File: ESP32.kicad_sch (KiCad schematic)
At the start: 5 parts, among them U1 ESP32-S3-WROOM-1

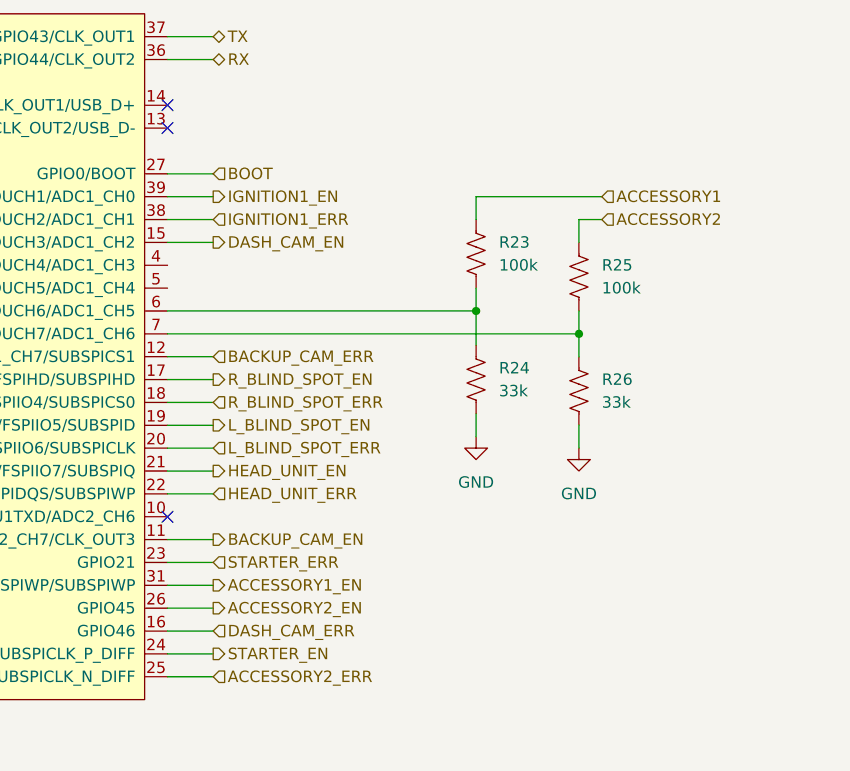
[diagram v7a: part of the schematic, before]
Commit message: add LED for debugging
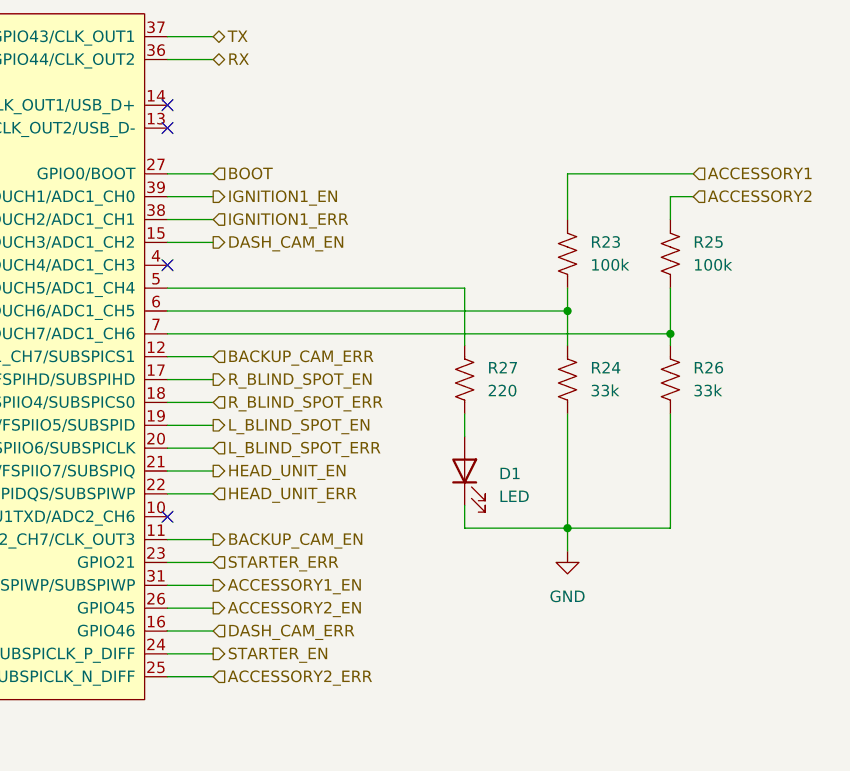
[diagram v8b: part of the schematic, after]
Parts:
- added D1: LED, LED_SMD:LED_0603_1608Metric, symbol Device:LED
- added R27: 220, Resistor_SMD:R_0603_1608Metric, symbol Device:R_US
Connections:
- net GND: now also D1.1 (K)
- net at U1.5 (GPIO5/TOUCH5/ADC1_CH4): now also R27.1
- new net: D1.2 (A), R27.2
- no-connect marks 7 -> 8
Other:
- moved on the sheet: R23, R24, R25, R26
